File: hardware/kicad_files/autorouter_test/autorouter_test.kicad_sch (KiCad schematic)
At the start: 7 parts, among them SW1 Tactile Switch

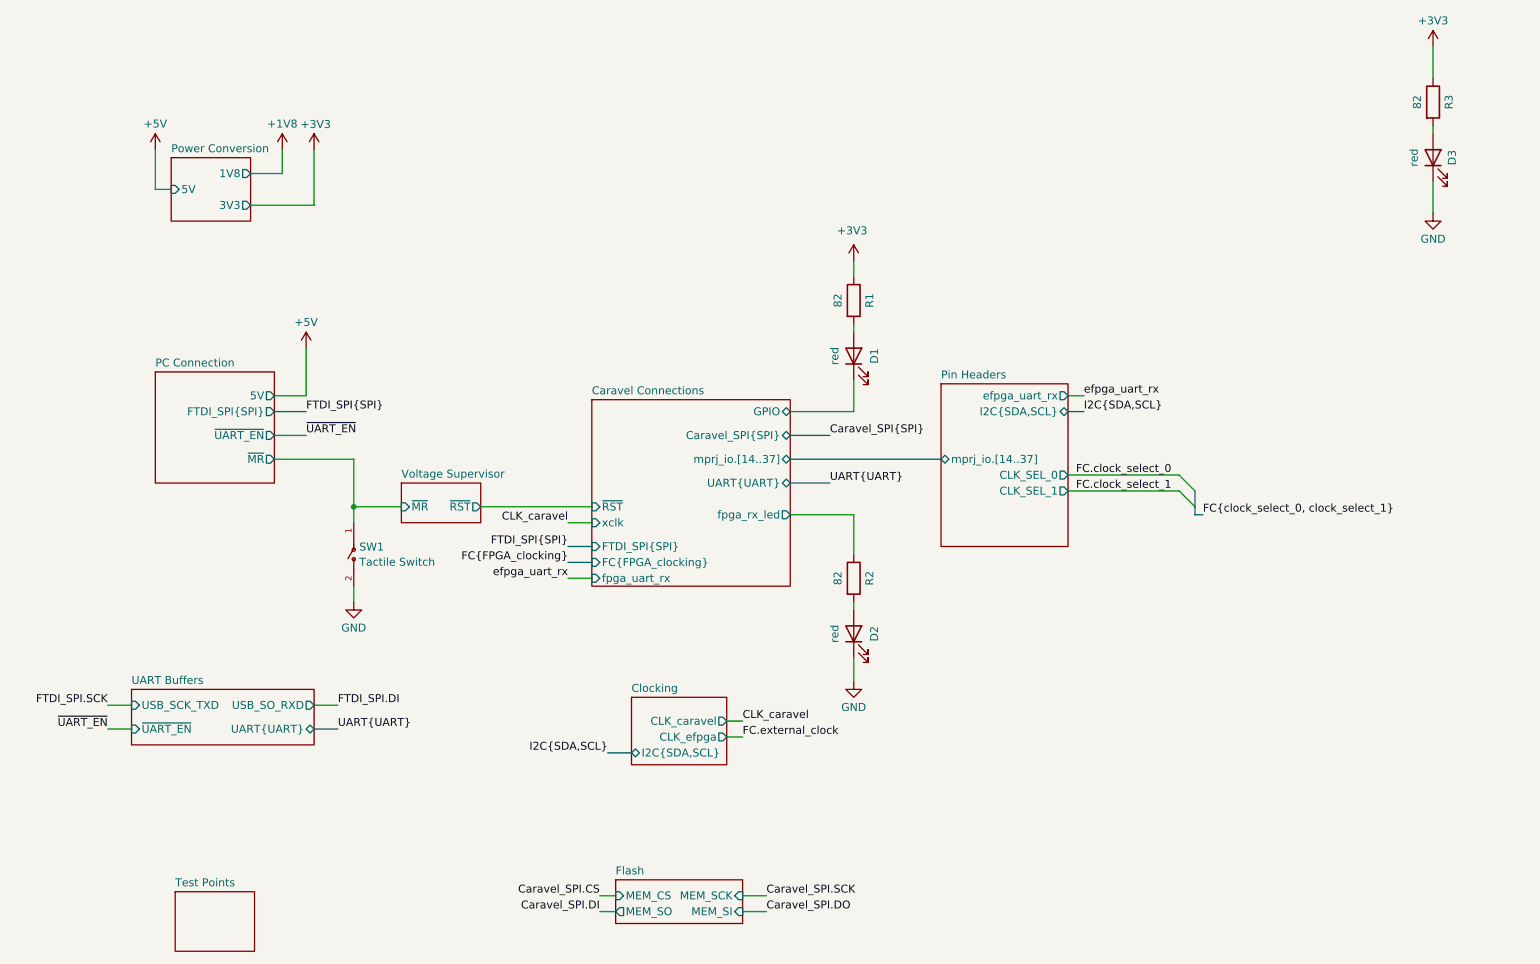
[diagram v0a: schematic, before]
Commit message: feat: first version of a complete layout. USB-C port might be problematic, FTDI chip does not have the best arrangement
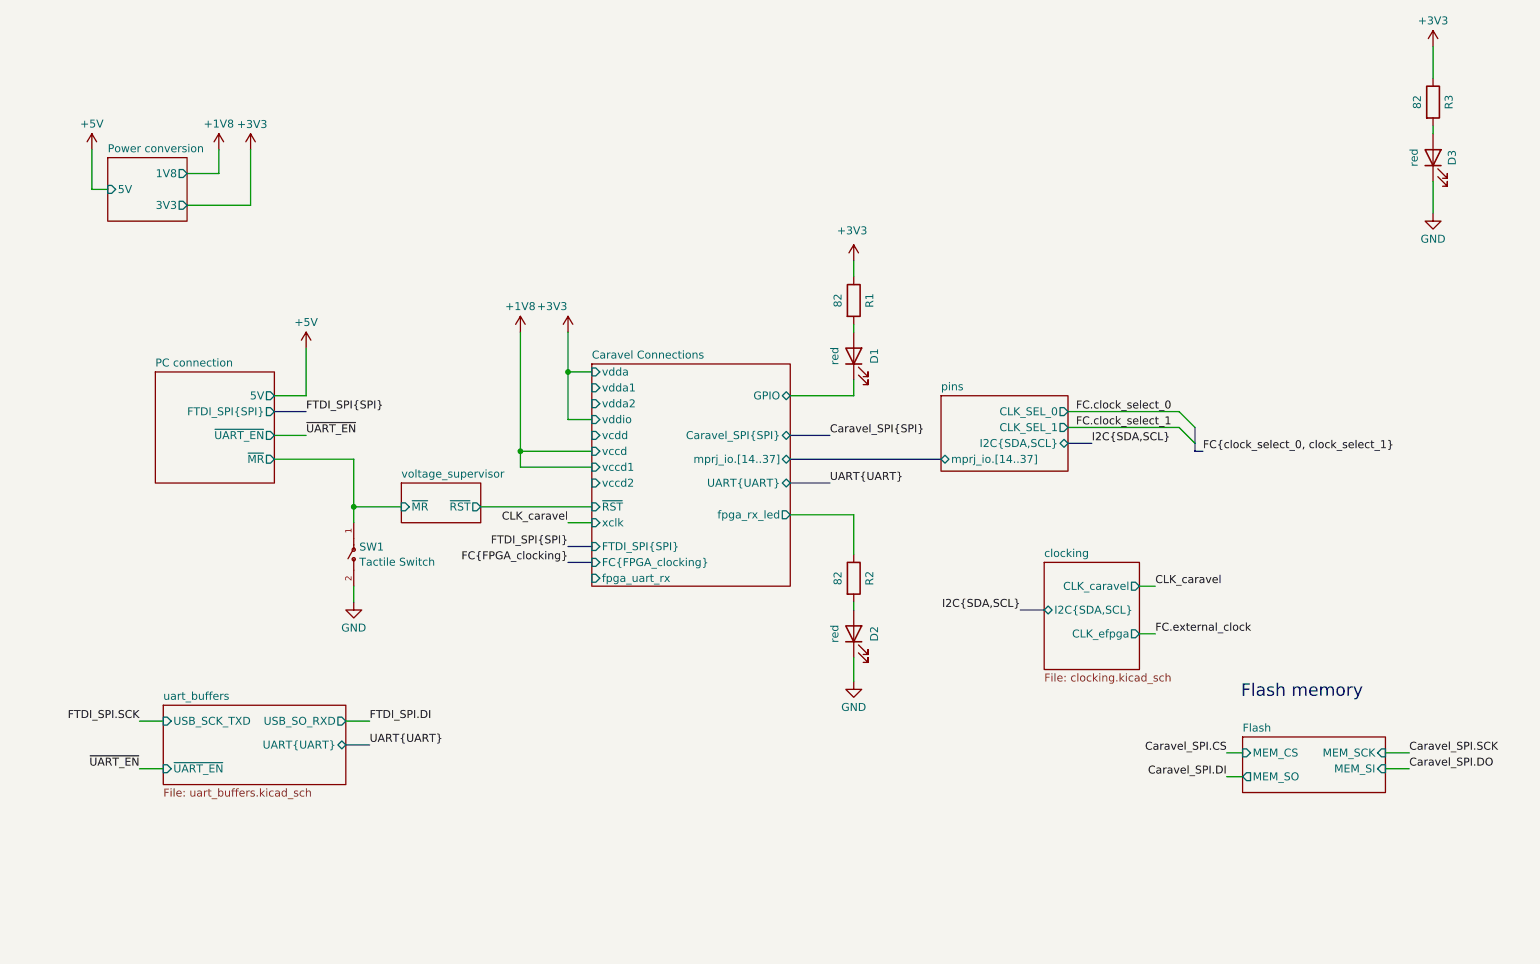
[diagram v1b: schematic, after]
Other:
- sheet Clocking renamed clocking
- sheet PC Connection renamed PC connection
- sheet Pin Headers renamed pins
- sheet Power Conversion renamed Power conversion
- sheet UART Buffers renamed uart_buffers
- sheet Voltage Supervisor renamed voltage_supervisor
- removed sheet Test Points
- sheet Caravel Connections ports: added vccd, vccd1, vccd2, vcdd, vdda, vdda1, vdda2, vddio; removed none
- sheet pins ports: added none; removed efpga_uart_rx
- note added: "Flash memory"
- title: FABulous Board -> FABulous board
